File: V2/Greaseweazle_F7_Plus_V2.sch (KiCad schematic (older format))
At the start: 71 parts, among them J1 Wurth 694106301002, J10 PIN1X2, J11 PIN1X2, J12 IDC Box Header, J2 USB_B, J3 Molex 105017-1001, J4 TE EI 171826-4, J5 PIN1X3, J6 PIN1X2, J7 PIN1X5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

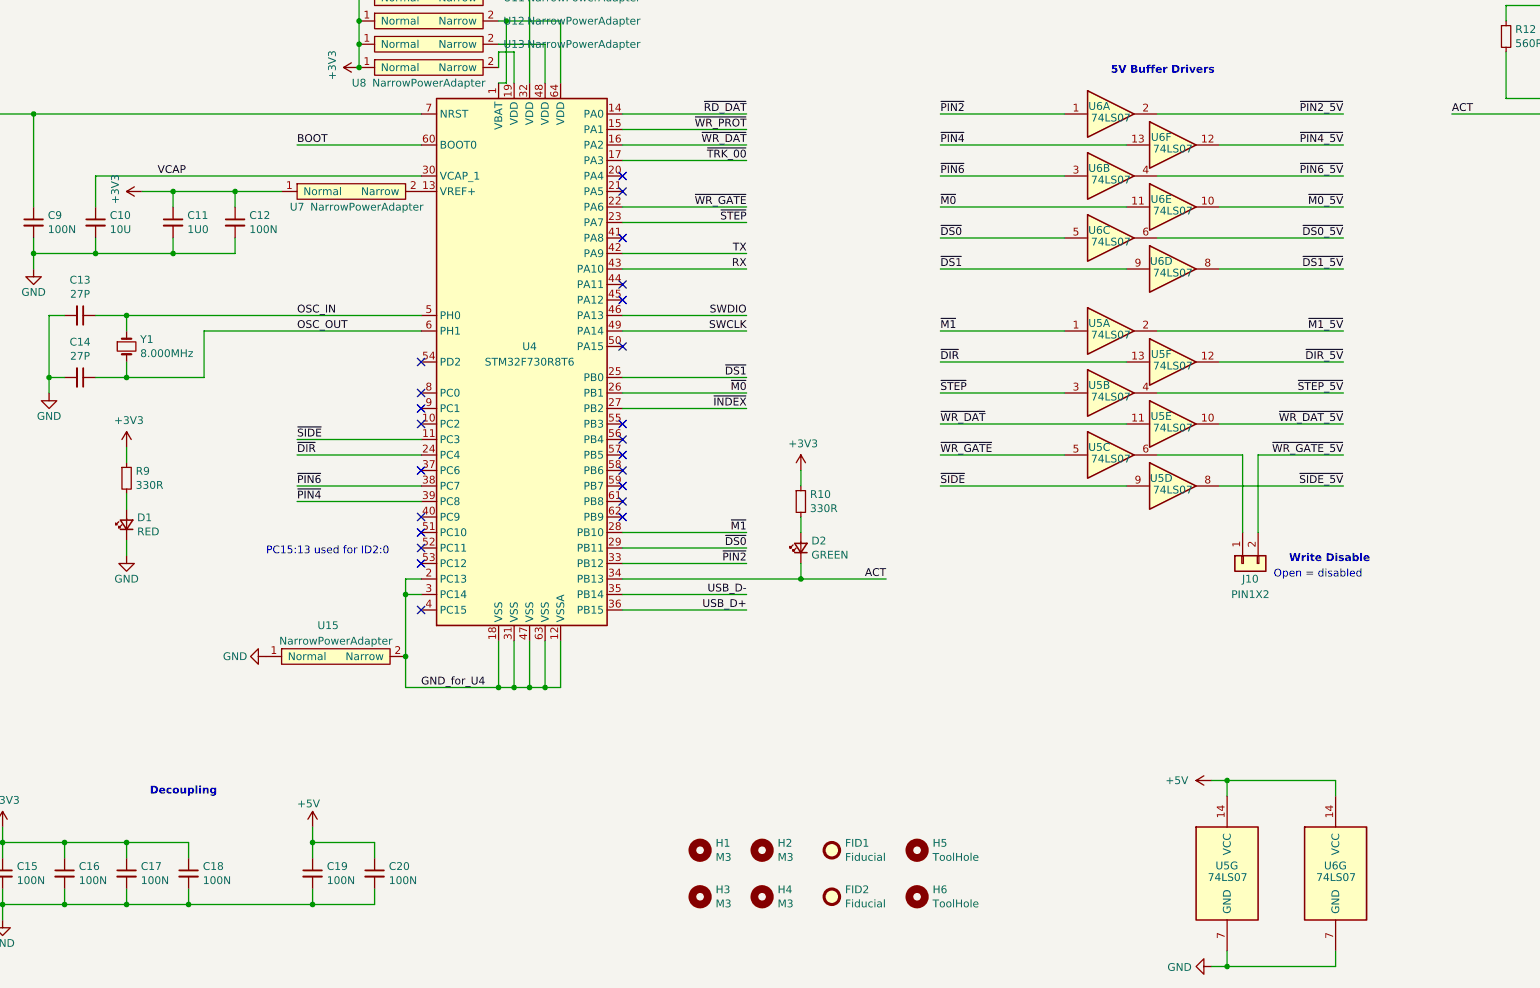
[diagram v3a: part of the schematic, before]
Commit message: changed C10 from 10u to 4.7u according to STM doc changed 74LS07 to 74LVC07APW,118 to reduce cost
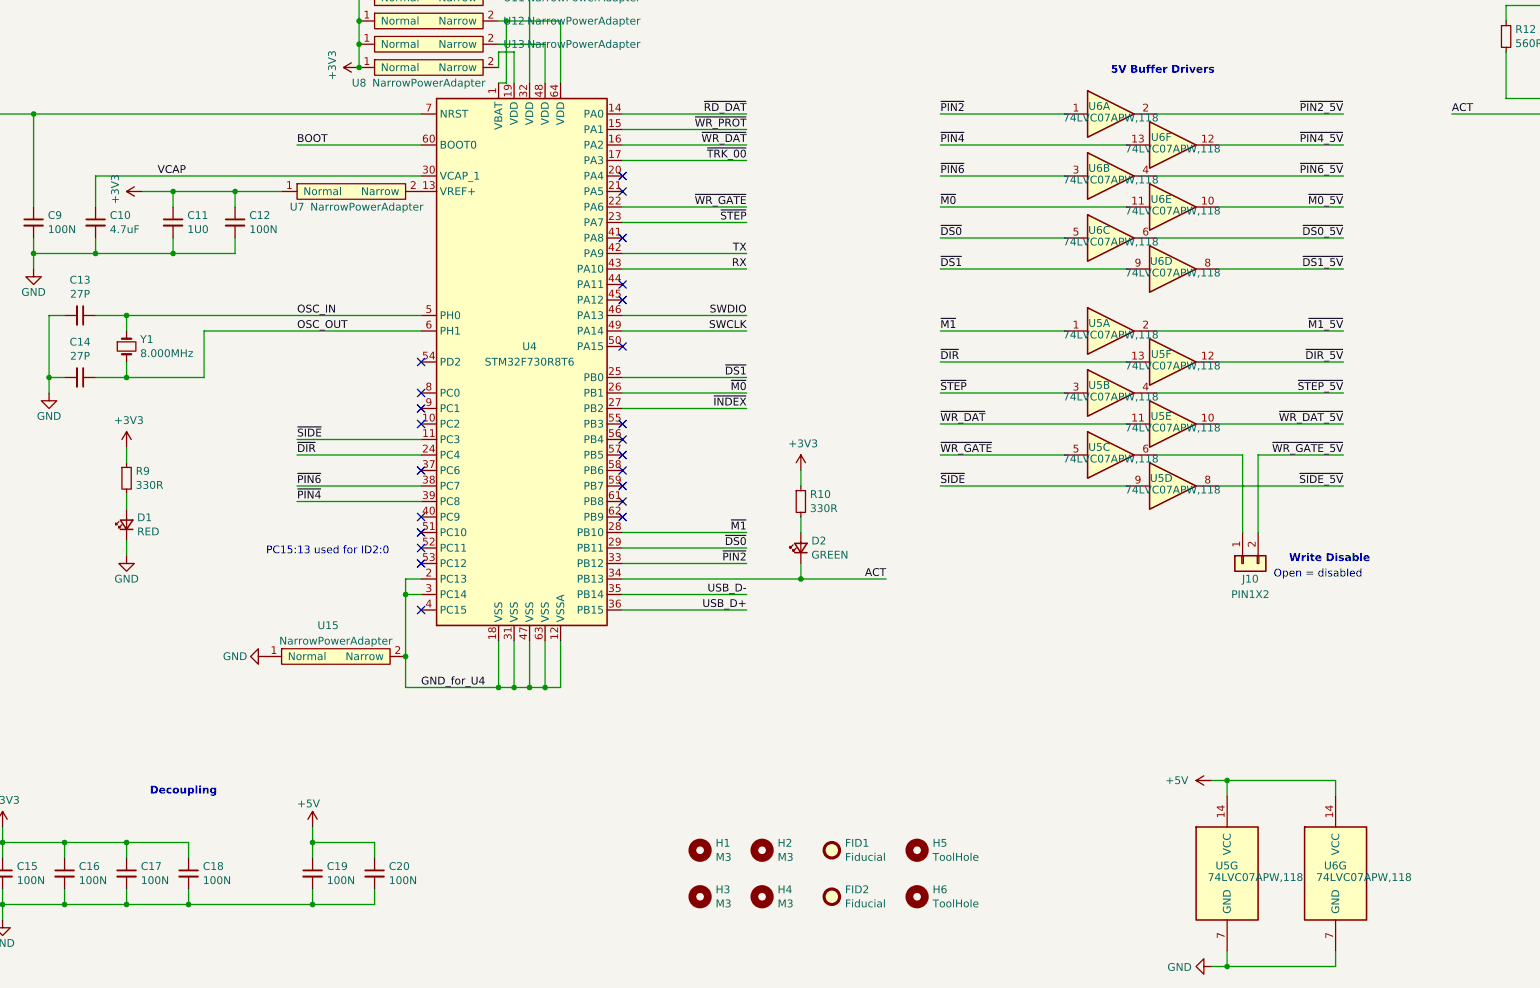
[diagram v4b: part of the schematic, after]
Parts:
- C10: value 10U -> 4.7uF; LCSC C15850 -> C1779; MFR.Part CL21A106KAYNNNE -> CL21A475KAQNNNE
- U5, U6: value 74LS07 -> 74LVC07APW,118; footprint Package_SO:SOIC-14_3.9x8.7mm_P1.27mm -> Package_SO:TSSOP-14_4.4x5mm_P0.65mm; LCSC C6801 -> C6051; MFR.Part SN74LS07DRG4 -> 74LVC07APW,118

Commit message: replaced 3.3V regulator by cheaper one moved many parts to make space
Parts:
- added R21: 220R, Resistor_SMD:R_0805_2012Metric, symbol Device:R_Small
- added R22: 330R, Resistor_SMD:R_0805_2012Metric, symbol Device:R_Small
- U2: value TLV75533PDBV -> LM317AG-TN3-R; footprint Package_TO_SOT_SMD:SOT-23-5 -> Package_TO_SOT_SMD:TO-252-2; symbol Regulator_Linear:TLV75533PDBV -> Regulator_Linear:LM317_TO-252; LCSC C404027 -> C75510; MFR.Part TLV75533PDBVR -> LM317AG-TN3-R
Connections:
- net +3V3: now also U2.2 (VO), R21.1; no longer U2.5 (OUT)
- net GND: now also R22.2; no longer U2.2 (GND)
- net USB_VBUS: no longer U2.1 (IN)
- new net: R21.2, R22.1, U2.1 (ADJ)
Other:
- moved on the sheet: C7, C8
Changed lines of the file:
@@
 Text Notes 3350 600  0    50   ~ 10
 5V Regulator
-$Comp
-L Device:C_Small C8
-U 1 1 5EE9AD0C
-P 4200 2900
-F 0 "C8" H 4292 2946 50  0000 L CNN
-F 1 "1U0" H 4292 2855 50  0000 L CNN
-F 2 "Capacitor_SMD:C_0402_1005Metric" H 4200 2900 50  0001 C CNN
-F 3 "https://datasheet.lcsc.com/szlcsc/Samsung-Electro-Mechanics-CL05A105KA5NQNC_C52923.pdf" H 4200 2900 50  0001 C CNN
-F 4 "C52923" H 4200 2900 50  0001 C CNN "LCSC"
-F 5 "CL05A105KA5NQNC" H 4200 2900 50  0001 C CNN "MFR.Part"
-	1    4200 2900
-	1    0    0    -1
-$EndComp
 Wire Wire Line
 	3100 1200 3200 1200
@@
 Connection ~ 2200 1000
 $Comp
-L Regulator_Linear:TLV75533PDBV U2
+L Regulator_Linear:LM317_TO-252 U2
 U 1 1 5F4F706B
 P 3600 2800
 F 0 "U2" H 3600 3142 50  0000 C CNN
-F 1 "TLV75533PDBV" H 3600 3051 50  0000 C CNN
-F 2 "Package_TO_SOT_SMD:SOT-23-5" H 3600 3125 50  0001 C CIN
-F 3 "https://datasheet.lcsc.com/szlcsc/1907311431_Texas-Instruments-TI-TLV75533PDBVR_C404027.pdf" H 3600 2850 50  0001 C CNN
-F 4 "C404027" H 3600 2800 50  0001 C CNN "LCSC"
-F 5 "TLV75533PDBVR" H 3600 2800 50  0001 C CNN "MFR.Part"
+F 1 "LM317AG-TN3-R" H 3600 3051 50  0000 C CNN
+F 2 "Package_TO_SOT_SMD:TO-252-2" H 3600 3125 50  0001 C CIN
+F 3 "https://datasheet.lcsc.com/szlcsc/Unisonic-Tech-LM317AG-TN3-R_C75510.pdf" H 3600 2850 50  0001 C CNN
+F 4 "C75510" H 3600 2800 50  0001 C CNN "LCSC"
+F 5 "LM317AG-TN3-R" H 3600 2800 50  0001 C CNN "MFR.Part"
 	1    3600 2800
 	1    0    0    -1
 $EndComp
 Wire Wire Line
-	3200 2700 3200 2800
-Wire Wire Line
-	3200 2800 3300 2800
-Connection ~ 3200 2700
-Wire Wire Line
-	3200 2700 3300 2700
-Wire Wire Line
-	2800 2700 2800 2800
-Wire Wire Line
-	2800 2700 3200 2700
-Wire Wire Line
-	2800 3000 2800 3200
-Wire Wire Line
-	2800 3200 3400 3200
-Wire Wire Line
-	3600 3200 3600 3100
-Wire Wire Line
-	3600 3200 4200 3200
-Wire Wire Line
-	4200 3200 4200 3000
-Connection ~ 3600 3200
-Wire Wire Line
-	3900 2700 4200 2700
-Wire Wire Line
-	4200 2700 4200 2800
+	2800 3400 3600 3400
 $Comp
 L power:+3V3 #PWR013
 U 1 1 5F5AA798
-P 4500 2700
-F 0 "#PWR013" H 4500 2550 50  0001 C CNN
-F 1 "+3V3" V 4500 2950 50  0000 C CNN
-F 2 "" H 4500 2700 50  0001 C CNN
-F 3 "" H 4500 2700 50  0001 C CNN
-	1    4500 2700
+P 4400 2800
+F 0 "#PWR013" H 4400 2650 50  0001 C CNN
+F 1 "+3V3" V 4400 3050 50  0000 C CNN
+F 2 "" H 4400 2800 50  0001 C CNN
+F 3 "" H 4400 2800 50  0001 C CNN
+	1    4400 2800
 	0    1    1    0
 $EndComp
-Wire Wire Line
-	4500 2700 4200 2700
-Connection ~ 4200 2700
 Text Notes 3400 2300 0    50   ~ 10
 3.3V Regulator
@@
 L power:GND #PWR0103
 U 1 1 5F185415
-P 3400 3300
-F 0 "#PWR0103" H 3400 3050 50  0001 C CNN
-F 1 "GND" H 3400 3150 50  0000 C CNN
-F 2 "" H 3400 3300 50  0001 C CNN
-F 3 "" H 3400 3300 50  0001 C CNN
-	1    3400 3300
-	1    0    0    -1
-$EndComp
-Wire Wire Line
-	3400 3300 3400 3200
-Connection ~ 3400 3200
-Wire Wire Line
-	3400 3200 3600 3200
+P 3600 3500
+F 0 "#PWR0103" H 3600 3250 50  0001 C CNN
+F 1 "GND" H 3600 3350 50  0000 C CNN
+F 2 "" H 3600 3500 50  0001 C CNN
+F 3 "" H 3600 3500 50  0001 C CNN
+	1    3600 3500
+	1    0    0    -1
+$EndComp
+Wire Wire Line
+	3600 3500 3600 3400
+Connection ~ 3600 3400
 Wire Wire Line
 	6850 8200 7400 8200
@@
 Wire Wire Line
 	14300 2000 14450 2000
-Text Label 2200 2700 0    50   ~ 0
+Text Label 2200 2800 0    50   ~ 0
 USB_VBUS
-Wire Wire Line
-	2800 2700 2200 2700
-Connection ~ 2800 2700
 Text Label 4200 1000 0    50   ~ 0
 SW
@@
 L Device:C_Small C7
 U 1 1 5F511C72
-P 2800 2900
-F 0 "C7" H 2892 2946 50  0000 L CNN
-F 1 "1U0" H 2892 2855 50  0000 L CNN
-F 2 "Capacitor_SMD:C_0402_1005Metric" H 2800 2900 50  0001 C CNN
-F 3 "https://datasheet.lcsc.com/szlcsc/Samsung-Electro-Mechanics-CL05A105KA5NQNC_C52923.pdf" H 2800 2900 50  0001 C CNN
-F 4 "C52923" H 2800 2900 50  0001 C CNN "LCSC"
-F 5 "CL05A105KA5NQNC" H 2800 2900 50  0001 C CNN "MFR.Part"
-	1    2800 2900
+P 2800 3100
+F 0 "C7" H 2892 3146 50  0000 L CNN
+F 1 "1U0" H 2892 3055 50  0000 L CNN
+F 2 "Capacitor_SMD:C_0402_1005Metric" H 2800 3100 50  0001 C CNN
+F 3 "https://datasheet.lcsc.com/szlcsc/Samsung-Electro-Mechanics-CL05A105KA5NQNC_C52923.pdf" H 2800 3100 50  0001 C CNN
+F 4 "C52923" H 2800 3100 50  0001 C CNN "LCSC"
+F 5 "CL05A105KA5NQNC" H 2800 3100 50  0001 C CNN "MFR.Part"
+	1    2800 3100
 	1    0    0    -1
 $EndComp
@@
 	1    0    0    -1
 $EndComp
+Wire Wire Line
+	2200 2800 2800 2800
+Wire Wire Line
+	2800 3000 2800 2800
+Connection ~ 2800 2800
+Wire Wire Line
+	2800 2800 3300 2800
+$Comp
+L Device:C_Small C8
+U 1 1 5EE9AD0C
+P 4400 3100
+F 0 "C8" H 4492 3146 50  0000 L CNN
+F 1 "1U0" H 4492 3055 50  0000 L CNN
+F 2 "Capacitor_SMD:C_0402_1005Metric" H 4400 3100 50  0001 C CNN
+F 3 "https://datasheet.lcsc.com/szlcsc/Samsung-Electro-Mechanics-CL05A105KA5NQNC_C52923.pdf" H 4400 3100 50  0001 C CNN
+F 4 "C52923" H 4400 3100 50  0001 C CNN "LCSC"
+F 5 "CL05A105KA5NQNC" H 4400 3100 50  0001 C CNN "MFR.Part"
+	1    4400 3100
+	1    0    0    -1
+$EndComp
+Wire Wire Line
+	4400 3000 4400 2800
+Connection ~ 4400 2800
+$Comp
+L Device:R_Small R21
+U 1 1 60E048AF
+P 4000 2950
+F 0 "R21" H 4059 2996 50  0000 L CNN
+F 1 "220R" H 4059 2905 50  0000 L CNN
+F 2 "Resistor_SMD:R_0805_2012Metric" H 4000 2950 50  0001 C CNN
+F 3 "https://datasheet.lcsc.com/szlcsc/Uniroyal-Elec-0805W8F2200T5E_C17557.pdf" H 4000 2950 50  0001 C CNN
+F 4 "C17557" H 4000 2950 50  0001 C CNN "LCSC"
+F 5 "0805W8F2200T5E" H 4000 2950 50  0001 C CNN "MFR.Part"
+	1    4000 2950
+	1    0    0    -1
+$EndComp
+$Comp
+L Device:R_Small R22
+U 1 1 60E2CB7C
+P 4000 3250
+F 0 "R22" H 4059 3296 50  0000 L CNN
+F 1 "330R" H 4059 3205 50  0000 L CNN
+F 2 "Resistor_SMD:R_0805_2012Metric" H 4000 3250 50  0001 C CNN
+F 3 "https://datasheet.lcsc.com/szlcsc/Uniroyal-Elec-0805W8F3300T5E_C17630.pdf" H 4000 3250 50  0001 C CNN
+F 4 "C17630" H 4000 3250 50  0001 C CNN "LCSC"
+F 5 "0805W8F3300T5E" H 4000 3250 50  0001 C CNN "MFR.Part"
+	1    4000 3250
+	1    0    0    -1
+$EndComp
+Wire Wire Line
+	3600 3100 4000 3100
+Wire Wire Line
+	4000 3100 4000 3150
+Wire Wire Line
+	3900 2800 4000 2800
+Wire Wire Line
+	4000 2850 4000 2800
+Connection ~ 4000 2800
+Wire Wire Line
+	4000 2800 4400 2800
+Wire Wire Line
+	4000 3050 4000 3100
+Connection ~ 4000 3100
+Wire Wire Line
+	4000 3350 4000 3400
+Connection ~ 4000 3400
+Wire Wire Line
+	4000 3400 4400 3400
+Wire Wire Line
+	3600 3400 4000 3400
+Wire Wire Line
+	2800 3200 2800 3400
+Wire Wire Line
+	4400 3200 4400 3400
 $EndSCHEMATC

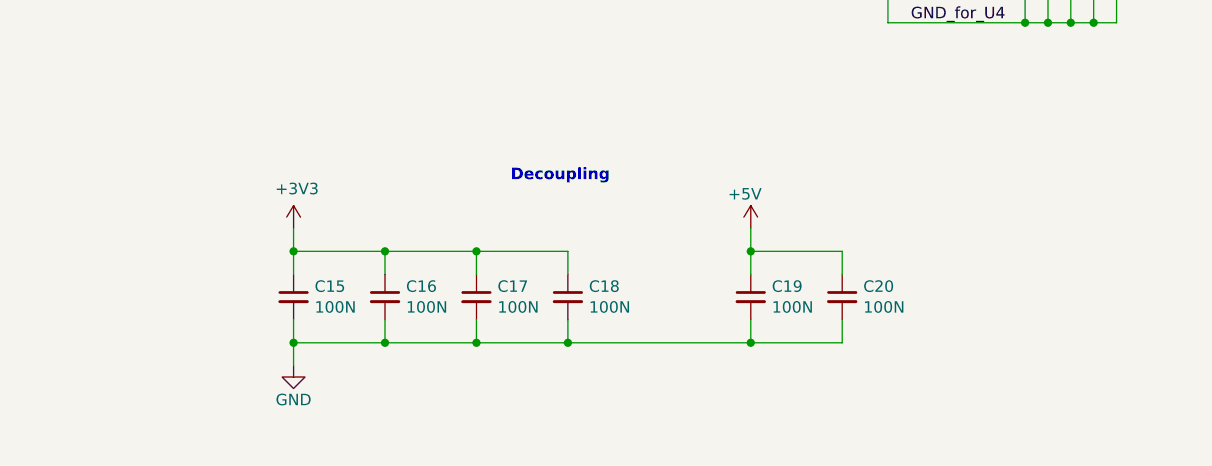
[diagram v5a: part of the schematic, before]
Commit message: added 3x 10000uF caps to buffer motor start of floppy which can draw up to 1A
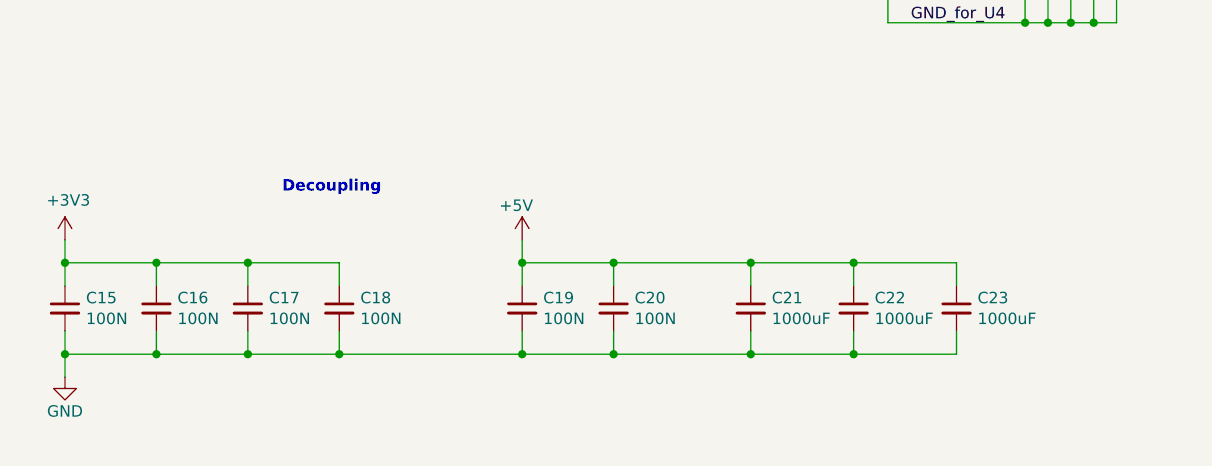
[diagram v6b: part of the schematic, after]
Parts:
- added C21, C22, C23: 1000uF, Capacitor_THT:C_Radial_D10.0mm_H20.0mm_P5.00mm, symbol Device:C_Small
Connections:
- net +5V: now also C21.1, C22.1, C23.1
- net GND: now also C21.2, C22.2, C23.2
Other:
- moved on the sheet: C15, C16, C17, C18, C19, C20

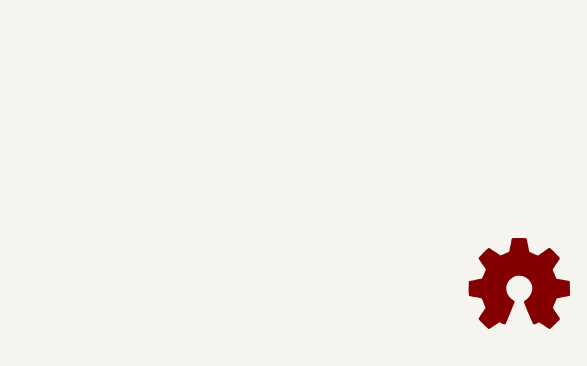
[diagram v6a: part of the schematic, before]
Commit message: fixed copyright and greaseweazel silk
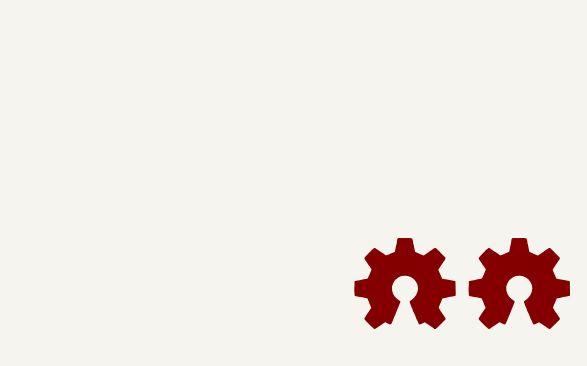
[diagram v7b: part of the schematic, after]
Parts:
- added LOGO2: Greaseweazle Logo, greaseweazle:Greaseweazle_Logo_verysmall, symbol Graphic:Logo_Open_Hardware_Small
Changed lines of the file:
@@
 Wire Wire Line
 	3700 9950 4150 9950
+$Comp
+L Graphic:Logo_Open_Hardware_Small LOGO2
+U 1 1 6142CF0C
+P 15400 10500
+F 0 "LOGO2" H 15400 10775 50  0001 C CNN
+F 1 "Greaseweazle Logo" H 15400 10275 50  0001 C CNN
+F 2 "greaseweazle:Greaseweazle_Logo_verysmall" H 15400 10500 50  0001 C CNN
+F 3 "~" H 15400 10500 50  0001 C CNN
+	1    15400 10500
+	1    0    0    -1
+$EndComp
 $EndSCHEMATC

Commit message: moved U11 NarrowPowCon to get better routing
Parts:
- LOGO2: value Greaseweazle Logo -> GW Logo
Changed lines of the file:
@@
 P 15400 10500
 F 0 "LOGO2" H 15400 10775 50  0001 C CNN
-F 1 "Greaseweazle Logo" H 15400 10275 50  0001 C CNN
+F 1 "GW Logo" H 15400 10275 50  0001 C CNN
 F 2 "greaseweazle:Greaseweazle_Logo_verysmall" H 15400 10500 50  0001 C CNN
 F 3 "~" H 15400 10500 50  0001 C CNN
